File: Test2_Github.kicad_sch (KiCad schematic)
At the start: 7 parts, among them SW1 SW_MEC_5G

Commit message: THT Footprint assigned
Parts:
- BT1, BT2: footprint (none) -> Connector_Molex:Molex_KK-396_A-41791-0002_1x02_P3.96mm_Vertical
- D1, D2: footprint (none) -> LED_THT:LED_D5.0mm_Clear
- R1, R2: footprint (none) -> Resistor_THT:R_Axial_DIN0204_L3.6mm_D1.6mm_P7.62mm_Horizontal
- SW1: footprint (none) -> Button_Switch_THT:SW_PUSH_6mm
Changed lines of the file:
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@@
       (effects (font (size 1.27 1.27)) (justify left))
     )
-    (property "Footprint" "" (at 114.3 96.52 0)
+    (property "Footprint" "LED_THT:LED_D5.0mm_Clear" (at 114.3 96.52 0)
       (effects (font (size 1.27 1.27)) hide)
     )
@@
       (effects (font (size 1.27 1.27)))
     )
-    (property "Footprint" "" (at 139.7 76.2 0)
+    (property "Footprint" "Button_Switch_THT:SW_PUSH_6mm" (at 139.7 76.2 0)
       (effects (font (size 1.27 1.27)) hide)
     )
@@
       (effects (font (size 1.27 1.27)) (justify left))
     )
-    (property "Footprint" "" (at 179.07 100.076 90)
+    (property "Footprint" "Connector_Molex:Molex_KK-396_A-41791-0002_1x02_P3.96mm_Vertical" (at 179.07 100.076 90)
       (effects (font (size 1.27 1.27)) hide)
     )
@@
       (effects (font (size 1.27 1.27)) (justify left))
     )
-    (property "Footprint" "" (at 115.316 108.204 90)
+    (property "Footprint" "Resistor_THT:R_Axial_DIN0204_L3.6mm_D1.6mm_P7.62mm_Horizontal" (at 115.316 108.204 90)
       (effects (font (size 1.27 1.27)) hide)
     )
@@
       (effects (font (size 1.27 1.27)) (justify left))
     )
-    (property "Footprint" "" (at 156.21 100.076 90)
+    (property "Footprint" "Connector_Molex:Molex_KK-396_A-41791-0002_1x02_P3.96mm_Vertical" (at 156.21 100.076 90)
       (effects (font (size 1.27 1.27)) hide)
     )
@@
       (effects (font (size 1.27 1.27)) (justify left))
     )
-    (property "Footprint" "" (at 124.46 96.52 0)
+    (property "Footprint" "LED_THT:LED_D5.0mm_Clear" (at 124.46 96.52 0)
       (effects (font (size 1.27 1.27)) hide)
     )
@@
       (effects (font (size 1.27 1.27)) (justify left))
     )
-    (property "Footprint" "" (at 125.476 108.204 90)
+    (property "Footprint" "Resistor_THT:R_Axial_DIN0204_L3.6mm_D1.6mm_P7.62mm_Horizontal" (at 125.476 108.204 90)
       (effects (font (size 1.27 1.27)) hide)
     )

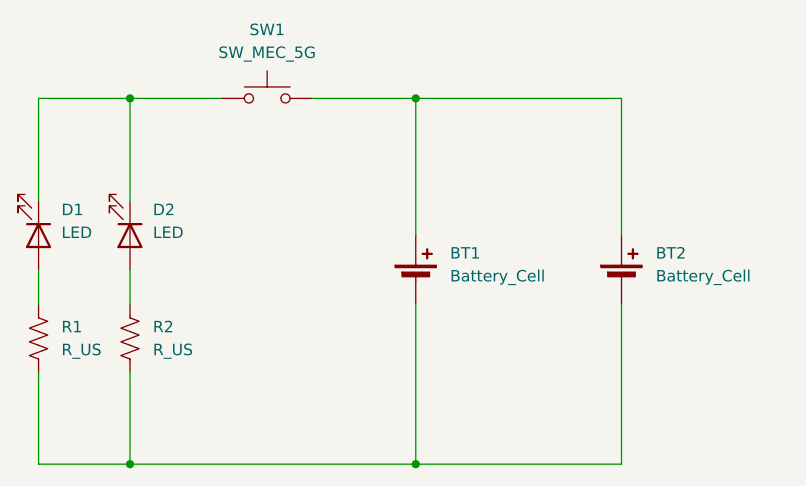
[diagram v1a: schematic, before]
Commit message: Push button symbol changed
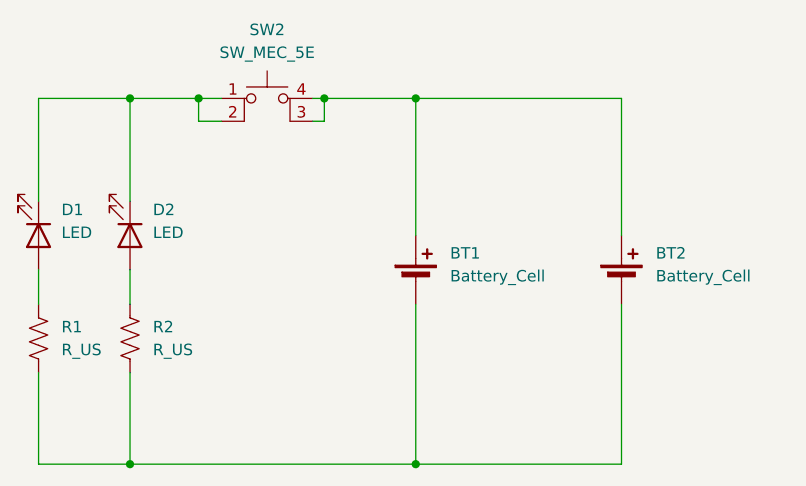
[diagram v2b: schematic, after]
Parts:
- removed SW1: SW_MEC_5G, Button_Switch_THT:SW_PUSH_6mm, symbol Switch:SW_MEC_5G
- added SW2: SW_MEC_5E, Button_Switch_THT:SW_PUSH_6mm, symbol Switch:SW_MEC_5E
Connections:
- net at D1.1 (K), D2.1 (K): now also SW2.1, SW2.2
- net at BT1.1 (+), BT2.1 (+): now also SW2.3 (K), SW2.4 (A)
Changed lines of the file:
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@@
 (kicad_sch (version 20230121) (generator eeschema)
   (paper "A4")
+  (junction (at 146.05 81.28) (diameter 0) (color 0 0 0 0)
+  )
+  (junction (at 132.08 81.28) (diameter 0) (color 0 0 0 0)
+  )
   (junction (at 124.46 121.92) (diameter 0) (color 0 0 0 0)
   )
@@
     (stroke (width 0) (type default))
   )
+  (wire (pts (xy 132.08 81.28) (xy 134.62 81.28))
+    (stroke (width 0) (type default))
+  )
   (wire (pts (xy 124.46 100.33) (xy 124.46 104.14))
     (stroke (width 0) (type default))
   )
   (wire (pts (xy 114.3 111.76) (xy 114.3 121.92))
+    (stroke (width 0) (type default))
+  )
+  (wire (pts (xy 146.05 83.82) (xy 146.05 81.28))
     (stroke (width 0) (type default))
   )
@@
     (stroke (width 0) (type default))
   )
+  (wire (pts (xy 146.05 81.28) (xy 156.21 81.28))
+    (stroke (width 0) (type default))
+  )
   (wire (pts (xy 124.46 81.28) (xy 124.46 92.71))
+    (stroke (width 0) (type default))
+  )
+  (wire (pts (xy 134.62 83.82) (xy 132.08 83.82))
     (stroke (width 0) (type default))
   )
@@
     (stroke (width 0) (type default))
   )
-  (wire (pts (xy 144.78 81.28) (xy 156.21 81.28))
+  (wire (pts (xy 144.78 81.28) (xy 146.05 81.28))
     (stroke (width 0) (type default))
   )
@@
     (stroke (width 0) (type default))
   )
+  (wire (pts (xy 132.08 83.82) (xy 132.08 81.28))
+    (stroke (width 0) (type default))
+  )
+  (wire (pts (xy 144.78 83.82) (xy 146.05 83.82))
+    (stroke (width 0) (type default))
+  )
   (wire (pts (xy 114.3 121.92) (xy 124.46 121.92))
     (stroke (width 0) (type default))
   )
-  (wire (pts (xy 124.46 81.28) (xy 134.62 81.28))
+  (wire (pts (xy 124.46 81.28) (xy 132.08 81.28))
     (stroke (width 0) (type default))
   )
@@
         (path "/dd405604-6c07-468b-817c-498d556835a8"
           (reference "D1") (unit 1)
-        )
-      )
-    )
-  )
-  (symbol (lib_id "Switch:SW_MEC_5G") (at 139.7 81.28 0) (unit 1)
-    (in_bom yes) (on_board yes) (dnp no) (fields_autoplaced)
-    (property "Reference" "SW1" (at 139.7 73.66 0)
-      (effects (font (size 1.27 1.27)))
-    )
-    (property "Value" "SW_MEC_5G" (at 139.7 76.2 0)
-      (effects (font (size 1.27 1.27)))
-    )
-    (property "Footprint" "Button_Switch_THT:SW_PUSH_6mm" (at 139.7 76.2 0)
-      (effects (font (size 1.27 1.27)) hide)
-    )
-    (property "Datasheet" "http://www.apem.com/int/index.php?controller=attachment&id_attachment=488" (at 139.7 76.2 0)
-      (effects (font (size 1.27 1.27)) hide)
-    )
-    (pin "4")
-    (pin "1")
-    (pin "3")
-    (pin "2")
-    (instances
-      (project "Test2_Github"
-        (path "/dd405604-6c07-468b-817c-498d556835a8"
-          (reference "SW1") (unit 1)
         )
       )
@@
         )
       )
+    )
+  )
+  (symbol (lib_id "Switch:SW_MEC_5E") (at 139.7 83.82 0) (unit 1)
+    (in_bom yes) (on_board yes) (dnp no) (fields_autoplaced)
+    (property "Reference" "SW2" (at 139.7 73.66 0)
+      (effects (font (size 1.27 1.27)))
+    )
+    (property "Value" "SW_MEC_5E" (at 139.7 76.2 0)
+      (effects (font (size 1.27 1.27)))
+    )
+    (property "Footprint" "Button_Switch_THT:SW_PUSH_6mm" (at 139.7 76.2 0)
+      (effects (font (size 1.27 1.27)) hide)
+    )
+    (property "Datasheet" "http://www.apem.com/int/index.php?controller=attachment&id_attachment=1371" (at 139.7 76.2 0)
+      (effects (font (size 1.27 1.27)) hide)
+    )
+    (pin "4")
+    (pin "3")
+    (pin "1")
+    (pin "2")
+    (instances
+      (project "Test2_Github"
+        (path "/dd405604-6c07-468b-817c-498d556835a8"
+          (reference "SW2") (unit 1)
+        )
+      )

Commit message: symbol edit the pin number as per footprint
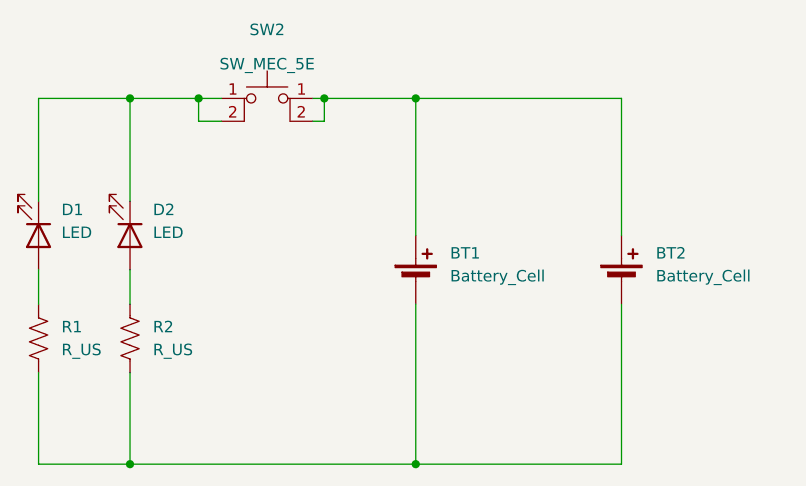
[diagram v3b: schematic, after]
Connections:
- net at BT1.1 (+), BT2.1 (+): now also SW2.1 (A), SW2.2 (K); no longer SW2.3 (K), SW2.4 (A)
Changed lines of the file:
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@@
   )
   (symbol (lib_id "Switch:SW_MEC_5E") (at 139.7 83.82 0) (unit 1)
-    (in_bom yes) (on_board yes) (dnp no) (fields_autoplaced)
+    (in_bom yes) (on_board yes) (dnp no)
     (property "Reference" "SW2" (at 139.7 73.66 0)
       (effects (font (size 1.27 1.27)))
     )
-    (property "Value" "SW_MEC_5E" (at 139.7 76.2 0)
+    (property "Value" "SW_MEC_5E" (at 139.7 77.47 0)
       (effects (font (size 1.27 1.27)))
     )
-    (property "Footprint" "Button_Switch_THT:SW_PUSH_6mm" (at 139.7 76.2 0)
+    (property "Footprint" "Button_Switch_THT:SW_PUSH_6mm" (at 139.7 68.58 0)
       (effects (font (size 1.27 1.27)) hide)
     )
-    (property "Datasheet" "http://www.apem.com/int/index.php?controller=attachment&id_attachment=1371" (at 139.7 76.2 0)
+    (property "Datasheet" "http://www.apem.com/int/index.php?controller=attachment&id_attachment=1371" (at 139.7 92.71 0)
       (effects (font (size 1.27 1.27)) hide)
     )
-    (pin "4")
-    (pin "3")
     (pin "1")
     (pin "2")
+    (pin "1")
+    (pin "2")

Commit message: Routing done
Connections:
- net at SW2.1 (A), SW2.2 (K): now also BT1.1 (+), BT2.1 (+); no longer D1.1 (K), D2.1 (K)
- net at R1.1: now also D1.1 (K); no longer D1.2 (A)
- net at D2.2 (A): now also D1.2 (A), SW2.1 (A), SW2.2 (K); no longer R2.1
- new net: D2.1 (K), R2.1
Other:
- moved on the sheet: D1, D2
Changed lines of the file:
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@@
     (stroke (width 0) (type default))
   )
-  (symbol (lib_id "Device:LED") (at 114.3 96.52 270) (unit 1)
+  (symbol (lib_id "Device:LED") (at 114.3 96.52 90) (unit 1)
     (in_bom yes) (on_board yes) (dnp no) (fields_autoplaced)
-    (property "Reference" "D1" (at 116.84 93.6625 90)
-      (effects (font (size 1.27 1.27)) (justify left))
+    (property "Reference" "D1" (at 118.11 96.8375 90)
+      (effects (font (size 1.27 1.27)) (justify right))
     )
-    (property "Value" "LED" (at 116.84 96.2025 90)
-      (effects (font (size 1.27 1.27)) (justify left))
+    (property "Value" "LED" (at 118.11 99.3775 90)
+      (effects (font (size 1.27 1.27)) (justify right))
     )
     (property "Footprint" "LED_THT:LED_D5.0mm_Clear" (at 114.3 96.52 0)
@@
     )
   )
-  (symbol (lib_id "Device:LED") (at 124.46 96.52 270) (unit 1)
+  (symbol (lib_id "Device:LED") (at 124.46 96.52 90) (unit 1)
     (in_bom yes) (on_board yes) (dnp no) (fields_autoplaced)
-    (property "Reference" "D2" (at 127 93.6625 90)
-      (effects (font (size 1.27 1.27)) (justify left))
+    (property "Reference" "D2" (at 128.27 96.8375 90)
+      (effects (font (size 1.27 1.27)) (justify right))
     )
-    (property "Value" "LED" (at 127 96.2025 90)
-      (effects (font (size 1.27 1.27)) (justify left))
+    (property "Value" "LED" (at 128.27 99.3775 90)
+      (effects (font (size 1.27 1.27)) (justify right))
     )
     (property "Footprint" "LED_THT:LED_D5.0mm_Clear" (at 124.46 96.52 0)
